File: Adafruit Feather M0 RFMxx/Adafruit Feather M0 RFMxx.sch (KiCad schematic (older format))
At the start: 39 parts, among them SW1 SPST_TACT-KMR2, U2 AP2112K-3.3, U3 MCP73831T-2ACI/OT, U4 RFM69HCW, X1 JSTPH, X2 32.768, X3 microUSB, X4 uFL

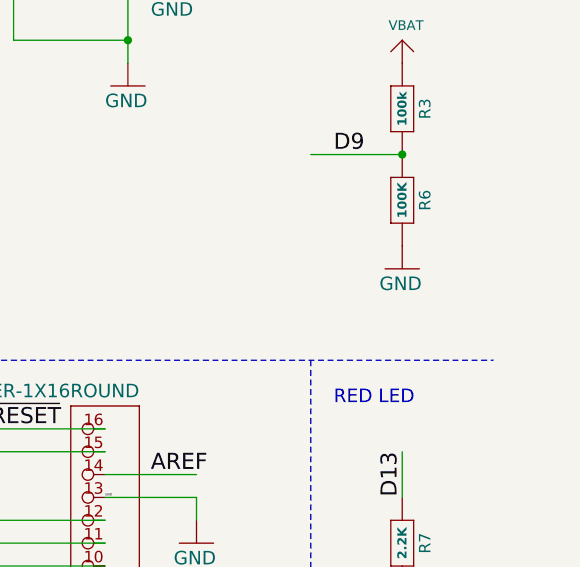
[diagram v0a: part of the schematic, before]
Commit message: Remaining Air wire was caused by ground pour on bottom that had become an island with the addition of the qwiic connector. Rerouted signals in that area to allow it to reconnect with other ground pour.
Now only "not connected" are defined ground area top and bottom.

Added gnd track between voltage sense resistor divider and ground so that it
shows when highlighting the GND net.

Moved track within USB connector to eliminate DRC "track too close to ..." error.

Now only 2 DRC errors are with holes in PCB that are part of X3 (USB connector).

Cleaned up silkscreen.

Plotted gerbers with option to not print silkscreen where there is no soldermask.
Option to not print silkscreen on pads did not seem to do anything.
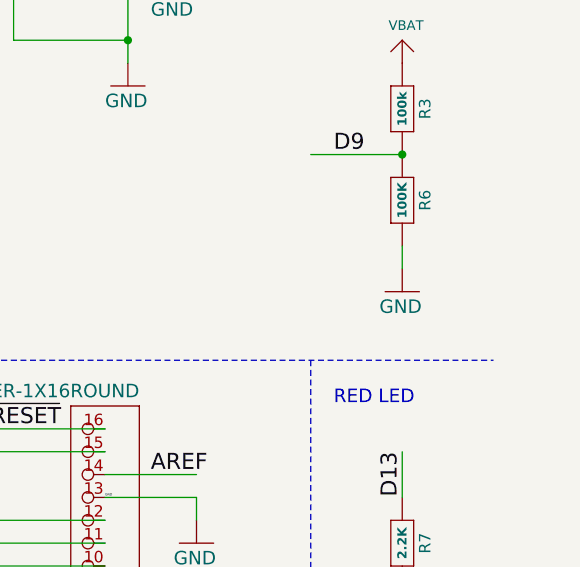
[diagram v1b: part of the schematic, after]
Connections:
- wire segments 160 -> 161
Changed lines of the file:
@@
 encoding utf-8
 Sheet 1 1
-Title ""
+Title "Adafruit Feather M0 LoRa plus qwiic"
 Date ""
-Rev ""
+Rev "v0.1"
 Comp ""
 Comment1 ""
@@
 L Adafruit_Feather_M0_RFMxx-eagle-import:GND #GND013
 U 1 0 1DDAFC179E3D6951
-P 13600 3700
-F 0 "#GND013" H 13600 3700 50  0001 C CNN
-F 1 "GND" H 13500 3600 59  0000 L BNN
-F 2 "" H 13600 3700 50  0001 C CNN
-F 3 "" H 13600 3700 50  0001 C CNN
-	1    13600 3700
+P 13600 3800
+F 0 "#GND013" H 13600 3800 50  0001 C CNN
+F 1 "GND" H 13500 3700 59  0000 L BNN
+F 2 "" H 13600 3800 50  0001 C CNN
+F 3 "" H 13600 3800 50  0001 C CNN
+	1    13600 3800
 	1    0    0    -1
 $EndComp
@@
 $EndComp
 $Comp
-L Adafruit_Feather_M0_RFMxx-eagle-import:+3V3 #+3V?
+L Adafruit_Feather_M0_RFMxx-eagle-import:+3V3 #+3V0101
 U 1 0 5C26B83D
 P 2400 1200
-F 0 "#+3V?" H 2400 1200 50  0001 C CNN
+F 0 "#+3V0101" H 2400 1200 50  0001 C CNN
 F 1 "+3V3" V 2300 1000 59  0000 L BNN
 F 2 "" H 2400 1200 50  0001 C CNN
@@
 $EndComp
 $Comp
-L Adafruit_Feather_M0_RFMxx-eagle-import:GND #U$?
+L Adafruit_Feather_M0_RFMxx-eagle-import:GND #U$0101
 U 1 0 5C26B88E
 P 1100 1300
-F 0 "#U$?" H 1100 1300 50  0001 C CNN
+F 0 "#U$0101" H 1100 1300 50  0001 C CNN
 F 1 "GND" H 1000 1200 59  0000 L BNN
 F 2 "" H 1100 1300 50  0001 C CNN
@@
 Text Label 2300 1600 0    50   ~ 0
 SCL
+Wire Wire Line
+	13600 3600 13600 3700
 $EndSCHEMATC

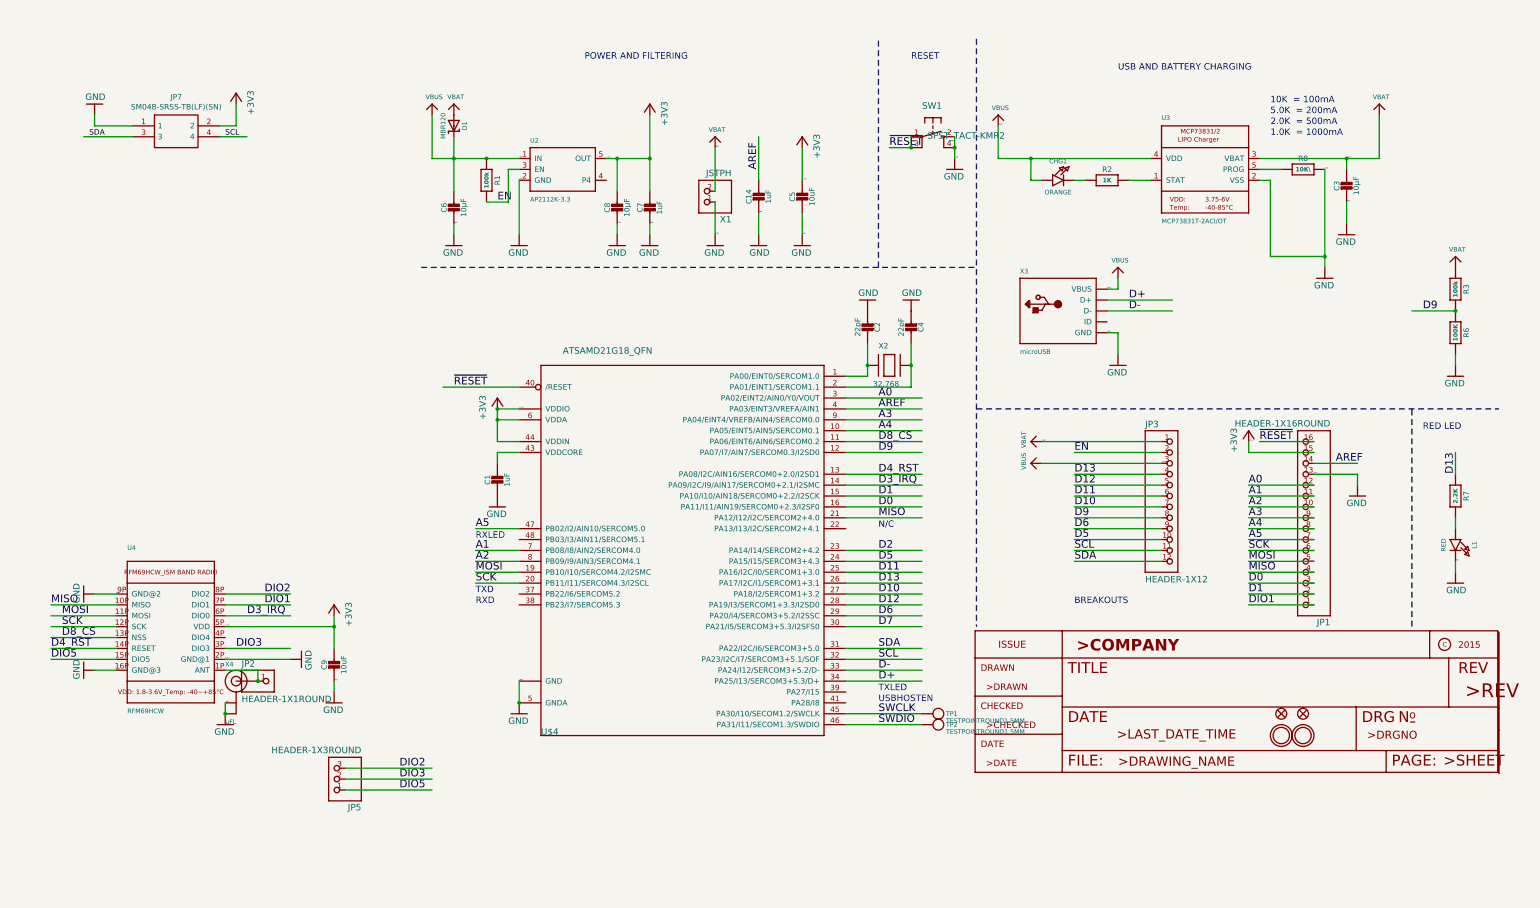
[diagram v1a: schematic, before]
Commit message: Added SPI flash from Adafruit Feather M0 Express. Still need to: - change 2 connections to RFM to other available pins - connect flash in schematic - route Note: the Netlist import complained about changing footprint for JP7 (qwiic connector)
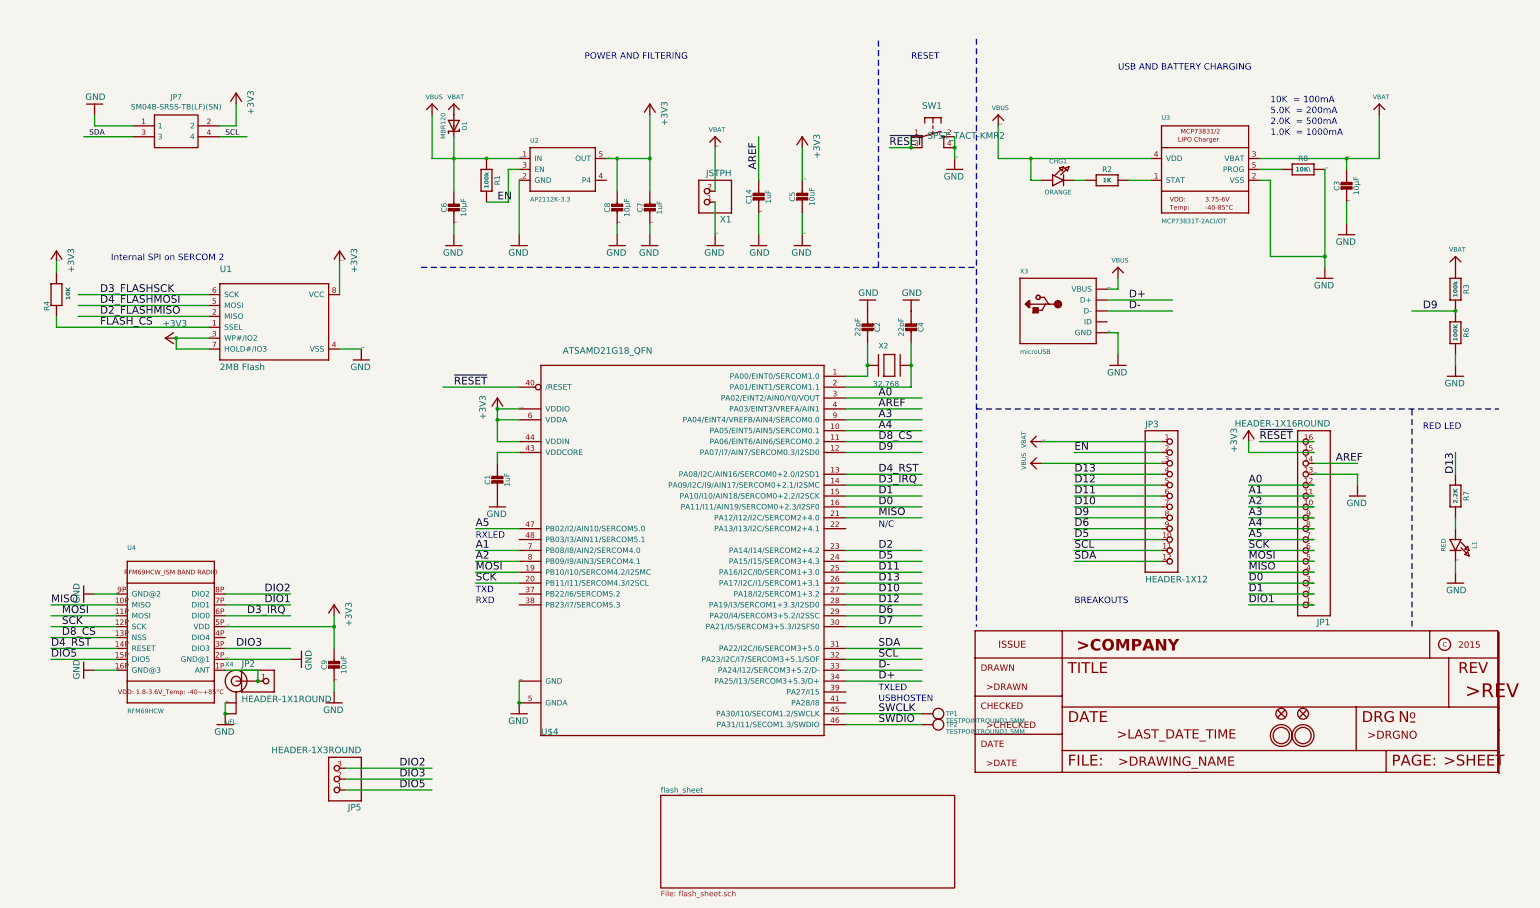
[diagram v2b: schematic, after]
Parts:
- added R4: 10K, Adafruit Feather M0 RFMxx:0603-NO, symbol Adafruit-Feather-M0-RFMxx-rescue:RESISTOR_0603_NOOUT-Adafruit_Feather_M0_Expres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
- added U1: 2MB Flash, Adafruit Feather M0 RFMxx:SOIC8_208MIL, symbol Adafruit-Feather-M0-RFMxx-rescue:SPIFLASH_SOIC8208MIL-Adafruit_Feather_M0_Expre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
- JP7: footprint SM04B-SRSS-TB(LFSN) -> SM04B-SRSS-TB(LF)(SN):SM04B-SRSS-TB(LFSN)
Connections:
- net labels added: D2_FLASHMISO, D3_FLASHSCK, D4_FLASHMOSI, FLASH_CS
- wire segments 161 -> 172
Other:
- note added: "Internal SPI on SERCOM 2"
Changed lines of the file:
@@
 EESchema Schematic File Version 4
 LIBS:Adafruit Feather M0 RFMxx-cache
+LIBS:Adafruit Feather M0 Express-cache
 EELAYER 26 0
 EELAYER END
 $Descr User 15021 8640
 encoding utf-8
-Sheet 1 1
+Sheet 1 2
 Title "Adafruit Feather M0 LoRa plus qwiic"
 Date ""
@@
 F 0 "JP7" H 1850 1765 50  0000 C CNN
 F 1 "SM04B-SRSS-TB(LF)(SN)" H 1850 1674 50  0000 C CNN
-F 2 "SM04B-SRSS-TB(LFSN)" H 2100 1600 50  0001 L CNN
+F 2 "SM04B-SRSS-TB(LF)(SN):SM04B-SRSS-TB(LFSN)" H 2100 1600 50  0001 L CNN
 F 3 "http://www.jst-mfg.com/product/pdf/eng/eSH.pdf" H 2100 1500 50  0001 L CNN
 F 4 "JST (JAPAN SOLDERLESS TERMINALS) - SM04B-SRSS-TB(LF)(SN) - CONNECTOR, HEADER, SMT, R/A, 1MM, 4WAY" H 2100 1400 50  0001 L CNN "Description"
@@
 Wire Wire Line
 	13600 3600 13600 3700
+$Sheet
+S 6300 7650 2700 850
+U 5C3457E2
+F0 "flash_sheet" 50
+F1 "flash_sheet.sch" 50
+$EndSheet
+Wire Wire Line
+	3550 3550 3350 3550
+Text Label 3550 3550 0    10   ~ 0
+GND
+Wire Wire Line
+	3350 2750 3350 3050
+Text Label 3350 2750 0    10   ~ 0
++3V3
+Wire Wire Line
+	2150 3450 1850 3450
+Wire Wire Line
+	1850 3450 1850 3550
+Wire Wire Line
+	1850 3550 2150 3550
+Connection ~ 1850 3450
+Text Label 2150 3450 0    10   ~ 0
++3V3
+Wire Wire Line
+	750  2750 750  2850
+Text Label 750  2750 0    10   ~ 0
++3V3
+Wire Wire Line
+	950  3150 2150 3150
+Text Label 1150 3150 0    70   ~ 0
+D4_FLASHMOSI
+Wire Wire Line
+	2150 3050 950  3050
+Text Label 1150 3050 0    70   ~ 0
+D3_FLASHSCK
+Wire Wire Line
+	750  3350 2150 3350
+Wire Wire Line
+	750  3250 750  3350
+Text Label 1150 3350 0    70   ~ 0
+FLASH_CS
+Wire Wire Line
+	2150 3250 950  3250
+Text Label 1150 3250 0    70   ~ 0
+D2_FLASHMISO
+$Comp
+L Adafruit-Feather-M0-RFMxx-rescue:SPIFLASH_SOIC8208MIL-Adafruit_Feather_M0_Express-eagle-import U?
+U 1 0 5C34E5AB
+P 2750 3350
+AR Path="/5C3457E2/5C34E5AB" Ref="U?"  Part="1"
+AR Path="/5C34E5AB" Ref="U1"  Part="1"
+F 0 "U1" H 2250 3850 59  0000 L BNN
+F 1 "2MB Flash" H 2250 2950 59  0000 L BNN
+F 2 "Adafruit Feather M0 RFMxx:SOIC8_208MIL" H 2750 3350 50  0001 C CNN
+F 3 "" H 2750 3350 50  0001 C CNN
+	1    2750 3350
+	1    0    0    -1
+$EndComp
+$Comp
+L Adafruit-Feather-M0-RFMxx-rescue:GND-Adafruit_Feather_M0_Express-eagle-import #U$?
+U 1 0 5C34E5B2
+P 3550 3650
+AR Path="/5C3457E2/5C34E5B2" Ref="#U$?"  Part="1"
+AR Path="/5C34E5B2" Ref="#U$0102"  Part="1"
+F 0 "#U$0102" H 3550 3650 50  0001 C CNN
+F 1 "GND" H 3450 3550 59  0000 L BNN
+F 2 "" H 3550 3650 50  0001 C CNN
+F 3 "" H 3550 3650 50  0001 C CNN
+	1    3550 3650
+	1    0    0    -1
+$EndComp
+$Comp
+L Adafruit-Feather-M0-RFMxx-rescue:RESISTOR_0603_NOOUT-Adafruit_Feather_M0_Express-eagle-import R?
+U 1 0 5C34E5B8
+P 750 3050
+AR Path="/5C3457E2/5C34E5B8" Ref="R?"  Part="1"
+AR Path="/5C34E5B8" Ref="R4"  Part="1"
+F 0 "R4" H 600 3109 50  0000 L BNN
+F 1 "10K" H 700 2920 40  0000 L BNB
+F 2 "Adafruit Feather M0 RFMxx:0603-NO" H 750 3050 50  0001 C CNN
+F 3 "" H 750 3050 50  0001 C CNN
+	1    750  3050
+	0    -1   -1   0
+$EndComp
+$Comp
+L Adafruit-Feather-M0-RFMxx-rescue:+3V3-Adafruit_Feather_M0_Express-eagle-import #+3V?
+U 1 0 5C34E5BF
+P 3350 2650
+AR Path="/5C3457E2/5C34E5BF" Ref="#+3V?"  Part="1"
+AR Path="/5C34E5BF" Ref="#+3V0102"  Part="1"
+F 0 "#+3V0102" H 3350 2650 50  0001 C CNN
+F 1 "+3V3" V 3250 2450 59  0000 L BNN
+F 2 "" H 3350 2650 50  0001 C CNN
+F 3 "" H 3350 2650 50  0001 C CNN
+	1    3350 2650
+	-1   0    0    -1
+$EndComp
+$Comp
+L Adafruit-Feather-M0-RFMxx-rescue:+3V3-Adafruit_Feather_M0_Express-eagle-import #+3V?
+U 1 0 5C34E5C5
+P 1750 3450
+AR Path="/5C3457E2/5C34E5C5" Ref="#+3V?"  Part="1"
+AR Path="/5C34E5C5" Ref="#+3V0103"  Part="1"
+F 0 "#+3V0103" H 1750 3450 50  0001 C CNN
+F 1 "+3V3" V 1650 3250 59  0000 L BNN
+F 2 "" H 1750 3450 50  0001 C CNN
+F 3 "" H 1750 3450 50  0001 C CNN
+	1    1750 3450
+	0    -1   1    0
+$EndComp
+$Comp
+L Adafruit-Feather-M0-RFMxx-rescue:+3V3-Adafruit_Feather_M0_Express-eagle-import #+3V?
+U 1 0 5C34E5CB
+P 750 2650
+AR Path="/5C3457E2/5C34E5CB" Ref="#+3V?"  Part="1"
+AR Path="/5C34E5CB" Ref="#+3V0104"  Part="1"
+F 0 "#+3V0104" H 750 2650 50  0001 C CNN
+F 1 "+3V3" V 650 2450 59  0000 L BNN
+F 2 "" H 750 2650 50  0001 C CNN
+F 3 "" H 750 2650 50  0001 C CNN
+	1    750  2650
+	-1   0    0    -1
+$EndComp
+Text Notes 1250 2750 0    59   ~ 0
+Internal SPI on SERCOM 2
 $EndSCHEMATC

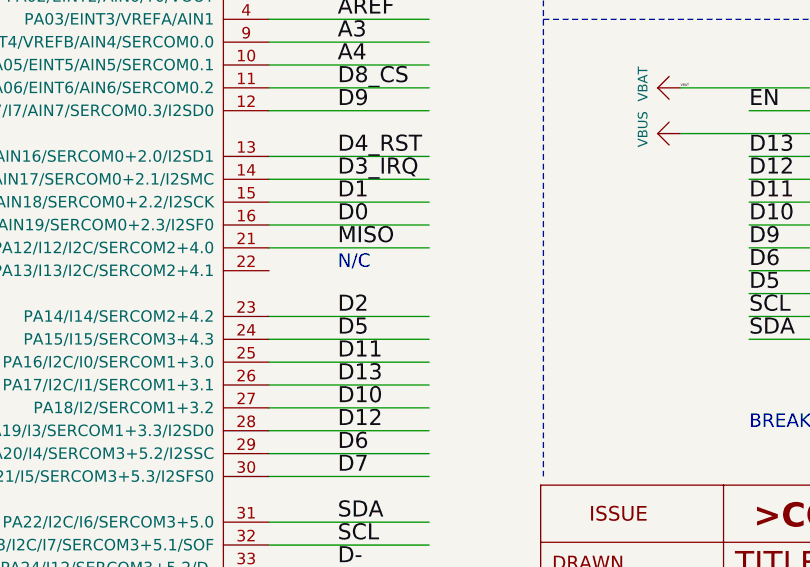
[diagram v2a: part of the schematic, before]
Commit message: Maybe in last commit: - Added spi flash footprint from Adafruit Feather M0 Express. - changed footprint of imported resistor for SPI flash to same as other 0603's.
Removed extraneous small track on SDA on TOP.
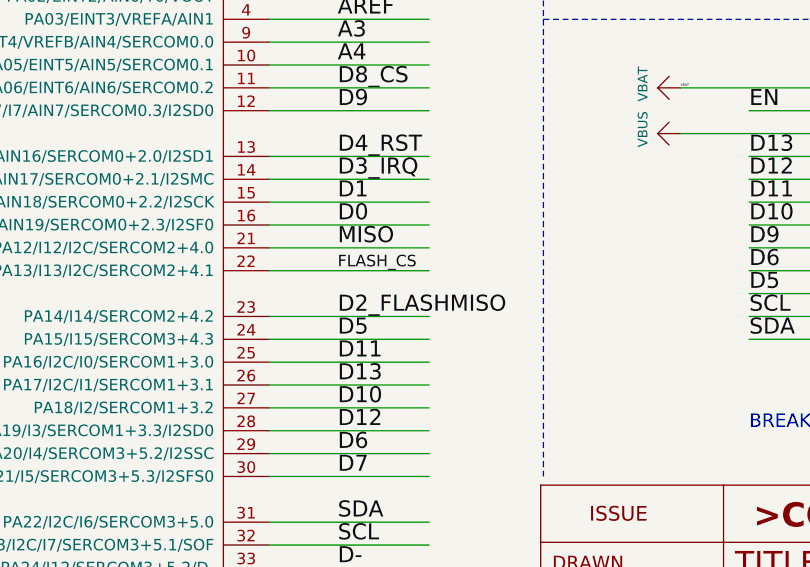
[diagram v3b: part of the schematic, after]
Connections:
- net labels removed: D2
- wire segments 172 -> 173
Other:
- note removed: "N/C"
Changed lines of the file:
@@
 EESchema Schematic File Version 4
 LIBS:Adafruit Feather M0 RFMxx-cache
-LIBS:Adafruit Feather M0 Express-cache
 EELAYER 26 0
 EELAYER END
@@
 	8000 5400 8700 5400
 Text Label 8300 5400 0    70   ~ 0
-D2
+D2_FLASHMISO
 Wire Wire Line
 	700  6300 1300 6300
@@
 Text Notes 11900 1600 0    59   ~ 0
 1.0K  = 1000mA
-Text Notes 8300 5200 0    59   ~ 0
-N/C
 Text Notes 8300 6700 0    59   ~ 0
 TXLED
@@
 Text Notes 1250 2750 0    59   ~ 0
 Internal SPI on SERCOM 2
+Text Label 8300 5200 0    50   ~ 0
+FLASH_CS
+Wire Wire Line
+	8000 5200 8700 5200
 $EndSCHEMATC

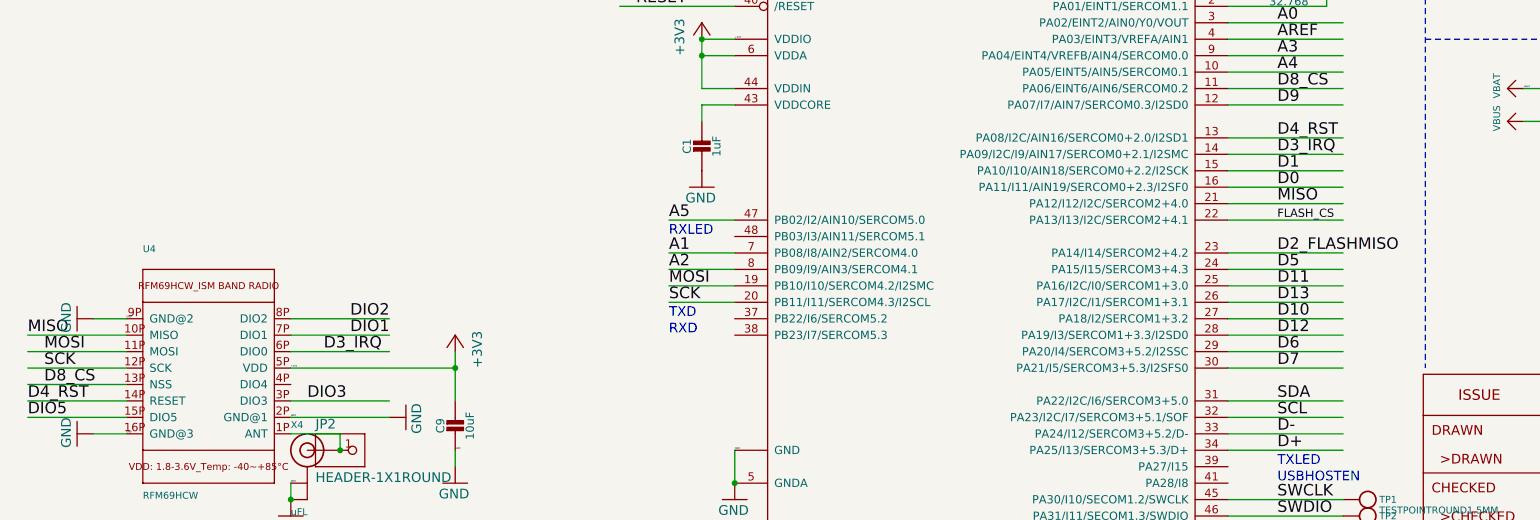
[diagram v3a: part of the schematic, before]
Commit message: New RST and IRQ lines chosen for RFM. Everything routed. DRC errors still to be fixed.
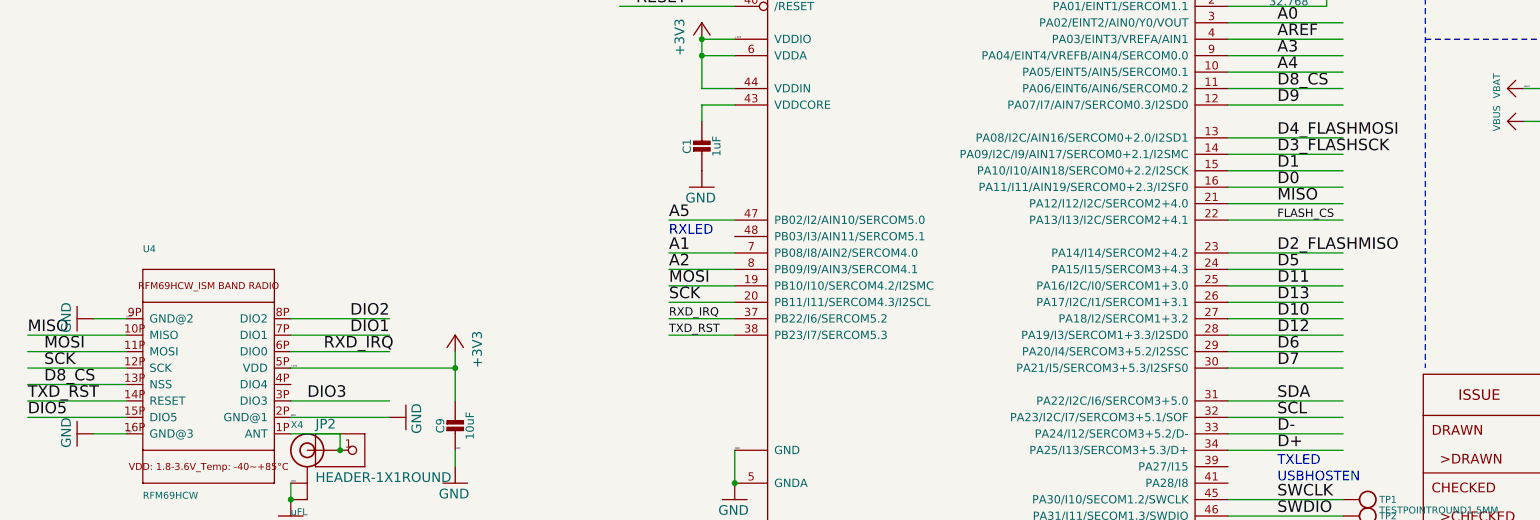
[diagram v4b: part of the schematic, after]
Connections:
- net labels added: RXD_IRQ, TXD_RST
- net labels removed: D3_IRQ, D4_RST
- wire segments 173 -> 175
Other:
- note removed: "RXD"
- note removed: "TXD"
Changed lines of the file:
@@
 	8000 4800 8700 4800
 Text Label 8300 4800 0    70   ~ 0
-D3_IRQ
+D3_FLASHSCK
 Wire Wire Line
 	2300 6000 2900 6000
 Text Label 2500 6000 0    70   ~ 0
-D3_IRQ
+RXD_IRQ
 Wire Wire Line
 	8000 5400 8700 5400
@@
 	700  6300 1300 6300
 Text Label 700  6300 0    70   ~ 0
-D4_RST
+TXD_RST
 Wire Wire Line
 	8700 4700 8000 4700
 Text Label 8300 4700 0    70   ~ 0
-D4_RST
+D4_FLASHMOSI
 Wire Wire Line
 	700  6200 1300 6200
@@
 Text Notes 4600 5300 0    59   ~ 0
 RXLED
-Text Notes 4600 5800 0    59   ~ 0
-TXD
-Text Notes 4600 5900 0    59   ~ 0
-RXD
 Text Notes 10500 1000 0    59   ~ 0
 USB AND BATTERY CHARGING
@@
 Wire Wire Line
 	8000 5200 8700 5200
+Wire Wire Line
+	4600 5900 5000 5900
+Wire Wire Line
+	5000 5800 4600 5800
+Text Label 4600 5900 0    50   ~ 0
+TXD_RST
+Text Label 4600 5800 0    50   ~ 0
+RXD_IRQ
 $EndSCHEMATC
